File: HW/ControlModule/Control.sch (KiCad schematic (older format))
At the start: 81 parts, among them J1 Conn_01x03, J2 Conn_01x03, J3 Conn_01x03, J4 Conn_01x03, J5 Conn_01x03, J6 Conn_01x03, J7 Conn_01x03, J8 Conn_01x03, U1 AD8629, U2 STM32L476VETx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

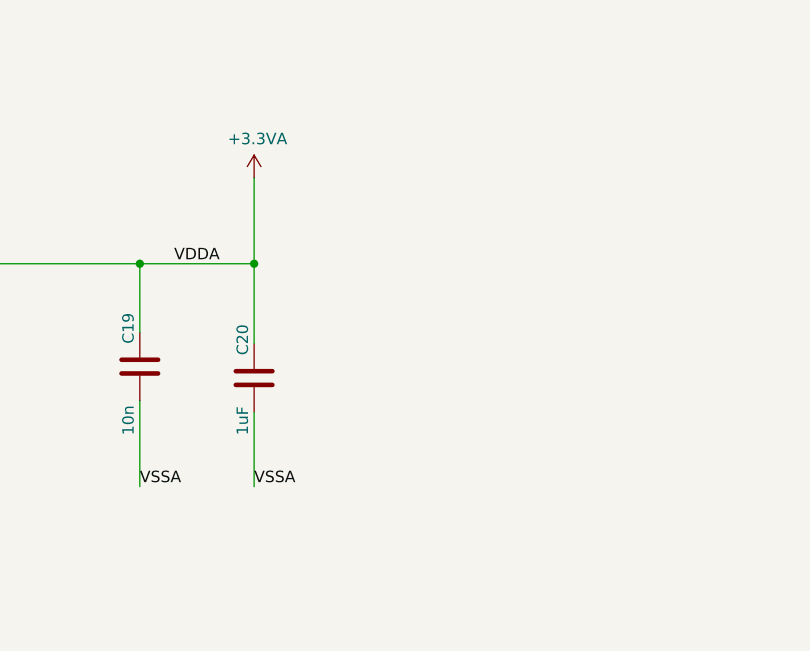
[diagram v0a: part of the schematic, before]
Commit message: Added Interafec IBOMS
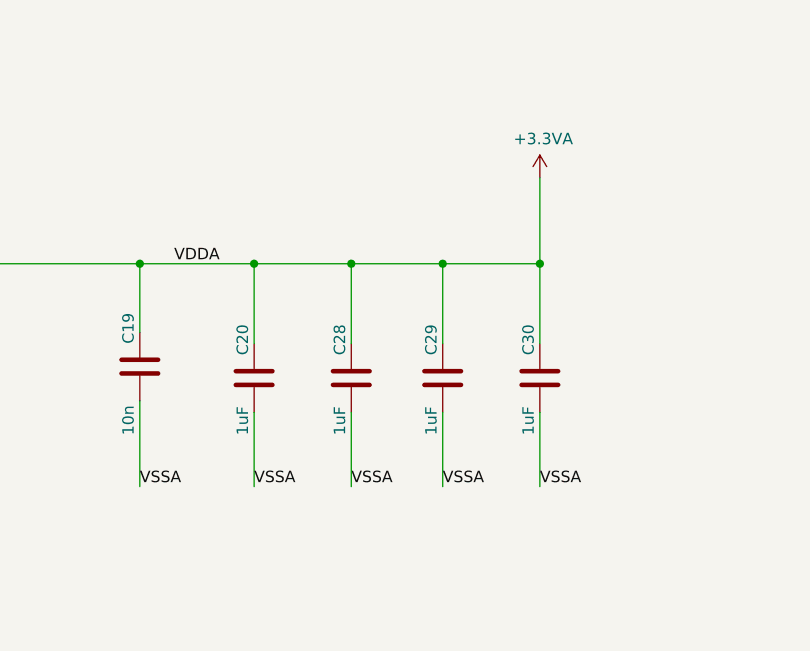
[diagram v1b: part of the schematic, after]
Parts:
- added C28, C29, C30: 1uF, Capacitor_SMD:C_0402_1005Metric, symbol Device:C
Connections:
- wire segments 308 -> 317
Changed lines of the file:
@@
 Connection ~ 10300 1650
-$Comp
-L power:+3.3VA #PWR030
-U 1 1 5E90E944
-P 14550 1450
-F 0 "#PWR030" H 14550 1300 50  0001 C CNN
-F 1 "+3.3VA" H 14565 1621 50  0000 C CNN
-F 2 "" H 14550 1450 50  0001 C CNN
-F 3 "" H 14550 1450 50  0001 C CNN
-	1    14550 1450
-	1    0    0    -1
-$EndComp
 $Comp
 L power:+3.3V #PWR012
@@
 	1    0    0    -1
 $EndComp
-Text Label 14200 1825 0    50   ~ 0
-VDDA
 Wire Wire Line
 	13100 1825 14050 1825
@@
 	14550 2475 14550 2800
 Wire Wire Line
-	14550 1450 14550 1825
-Wire Wire Line
 	10300 1550 10300 1650
 Wire Wire Line
@@
 Text Notes 7950 11850 0    197  ~ 0
 Voltage Regulator and Voltage Reference
+Wire Wire Line
+	14975 2475 14975 2800
+Text Label 14975 2800 0    50   ~ 0
+VSSA
+Wire Wire Line
+	14975 1825 14975 2175
+Wire Wire Line
+	15375 2475 15375 2800
+Text Label 15375 2800 0    50   ~ 0
+VSSA
+Wire Wire Line
+	15375 1825 15375 2175
+Wire Wire Line
+	15800 2475 15800 2800
+Text Label 15800 2800 0    50   ~ 0
+VSSA
+Wire Wire Line
+	15800 1825 15800 2175
+Wire Wire Line
+	14550 1825 14975 1825
+Connection ~ 14975 1825
+Wire Wire Line
+	14975 1825 15375 1825
+Connection ~ 15375 1825
+Wire Wire Line
+	15375 1825 15800 1825
+$Comp
+L Device:C C30
+U 1 1 5D5424B0
+P 15800 2325
+F 0 "C30" V 15750 2425 50  0000 L CNN
+F 1 "1uF" V 15750 2075 50  0000 L CNN
+F 2 "Capacitor_SMD:C_0402_1005Metric" H 15838 2175 50  0001 C CNN
+F 3 "~" H 15800 2325 50  0001 C CNN
+	1    15800 2325
+	1    0    0    -1
+$EndComp
+$Comp
+L Device:C C29
+U 1 1 5D527759
+P 15375 2325
+F 0 "C29" V 15325 2425 50  0000 L CNN
+F 1 "1uF" V 15325 2075 50  0000 L CNN
+F 2 "Capacitor_SMD:C_0402_1005Metric" H 15413 2175 50  0001 C CNN
+F 3 "~" H 15375 2325 50  0001 C CNN
+	1    15375 2325
+	1    0    0    -1
+$EndComp
+$Comp
+L Device:C C28
+U 1 1 5D50AF0D
+P 14975 2325
+F 0 "C28" V 14925 2425 50  0000 L CNN
+F 1 "1uF" V 14925 2075 50  0000 L CNN
+F 2 "Capacitor_SMD:C_0402_1005Metric" H 15013 2175 50  0001 C CNN
+F 3 "~" H 14975 2325 50  0001 C CNN
+	1    14975 2325
+	1    0    0    -1
+$EndComp
+Text Label 14200 1825 0    50   ~ 0
+VDDA
+Wire Wire Line
+	15800 1450 15800 1825
+$Comp
+L power:+3.3VA #PWR030
+U 1 1 5E90E944
+P 15800 1450
+F 0 "#PWR030" H 15800 1300 50  0001 C CNN
+F 1 "+3.3VA" H 15815 1621 50  0000 C CNN
+F 2 "" H 15800 1450 50  0001 C CNN
+F 3 "" H 15800 1450 50  0001 C CNN
+	1    15800 1450
+	1    0    0    -1
+$EndComp
+Connection ~ 15800 1825
 $EndSCHEMATC

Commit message: Created STM32L476 project
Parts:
- U_BTN1, U_BTN2, U_BTN3, U_BTN5: symbol Tactile_SPST-NO:Tactile_Switch_SPST-NO -> ControlModule-rescue:Tactile_Switch_SPST-NO-Tactile_SPST-NO
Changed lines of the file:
@@
 	19825 11300 19950 11300
 $Comp
-L Tactile_SPST-NO:Tactile_Switch_SPST-NO U_BTN3
+L ControlModule-rescue:Tactile_Switch_SPST-NO-Tactile_SPST-NO U_BTN3
 U 1 1 5CB3B653
 P 4600 13150
+AR Path="/5CB3B653" Ref="U_BTN3"  Part="1"
+AR Path="/5D061C98/5CB3B653" Ref="U_BTN3"  Part="1"
 F 0 "U_BTN3" H 4600 13550 50  0000 C CNN
 F 1 "Tactile_Switch_SPST-NO" H 4650 13450 50  0000 C CNN
@@
 NoConn ~ 5000 13250
 $Comp
-L Tactile_SPST-NO:Tactile_Switch_SPST-NO U_BTN5
+L ControlModule-rescue:Tactile_Switch_SPST-NO-Tactile_SPST-NO U_BTN5
 U 1 1 5CBE308F
 P 5850 13150
+AR Path="/5CBE308F" Ref="U_BTN5"  Part="1"
+AR Path="/5D061C98/5CBE308F" Ref="U_BTN5"  Part="1"
 F 0 "U_BTN5" H 5850 13550 50  0000 C CNN
 F 1 "Tactile_Switch_SPST-NO" H 5900 13450 50  0000 C CNN
@@
 NoConn ~ 6250 13250
 $Comp
-L Tactile_SPST-NO:Tactile_Switch_SPST-NO U_BTN2
+L ControlModule-rescue:Tactile_Switch_SPST-NO-Tactile_SPST-NO U_BTN2
 U 1 1 5CC20FAA
 P 2050 13150
+AR Path="/5CC20FAA" Ref="U_BTN2"  Part="1"
+AR Path="/5D061C98/5CC20FAA" Ref="U_BTN2"  Part="1"
 F 0 "U_BTN2" H 2050 13550 50  0000 C CNN
 F 1 "Tactile_Switch_SPST-NO" H 2100 13450 50  0000 C CNN
@@
 NoConn ~ 2450 13250
 $Comp
-L Tactile_SPST-NO:Tactile_Switch_SPST-NO U_BTN1
+L ControlModule-rescue:Tactile_Switch_SPST-NO-Tactile_SPST-NO U_BTN1
 U 1 1 5CC42781
 P 3350 13150
+AR Path="/5CC42781" Ref="U_BTN1"  Part="1"
+AR Path="/5D061C98/5CC42781" Ref="U_BTN1"  Part="1"
 F 0 "U_BTN1" H 3350 13550 50  0000 C CNN
 F 1 "Tactile_Switch_SPST-NO" H 3400 13450 50  0000 C CNN

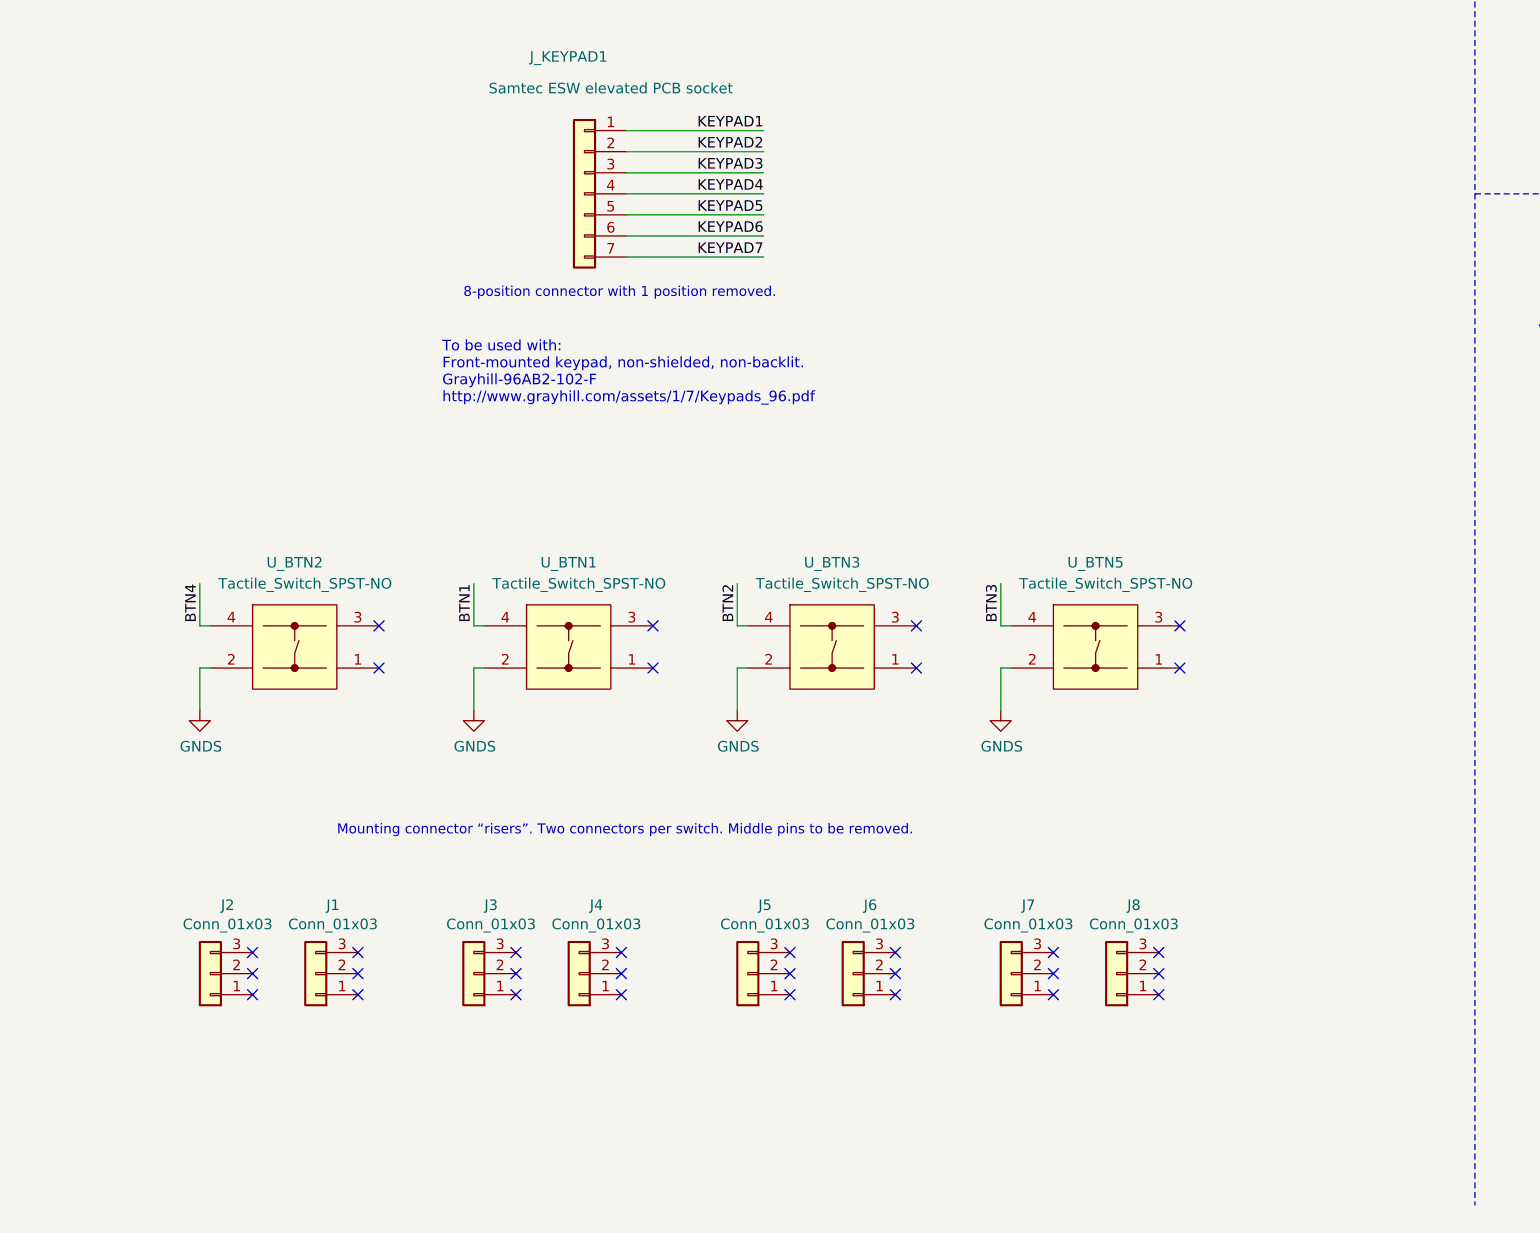
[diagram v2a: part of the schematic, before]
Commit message: debugged HW issue with EXTI buttons
- Buttons required external pull-up resistors
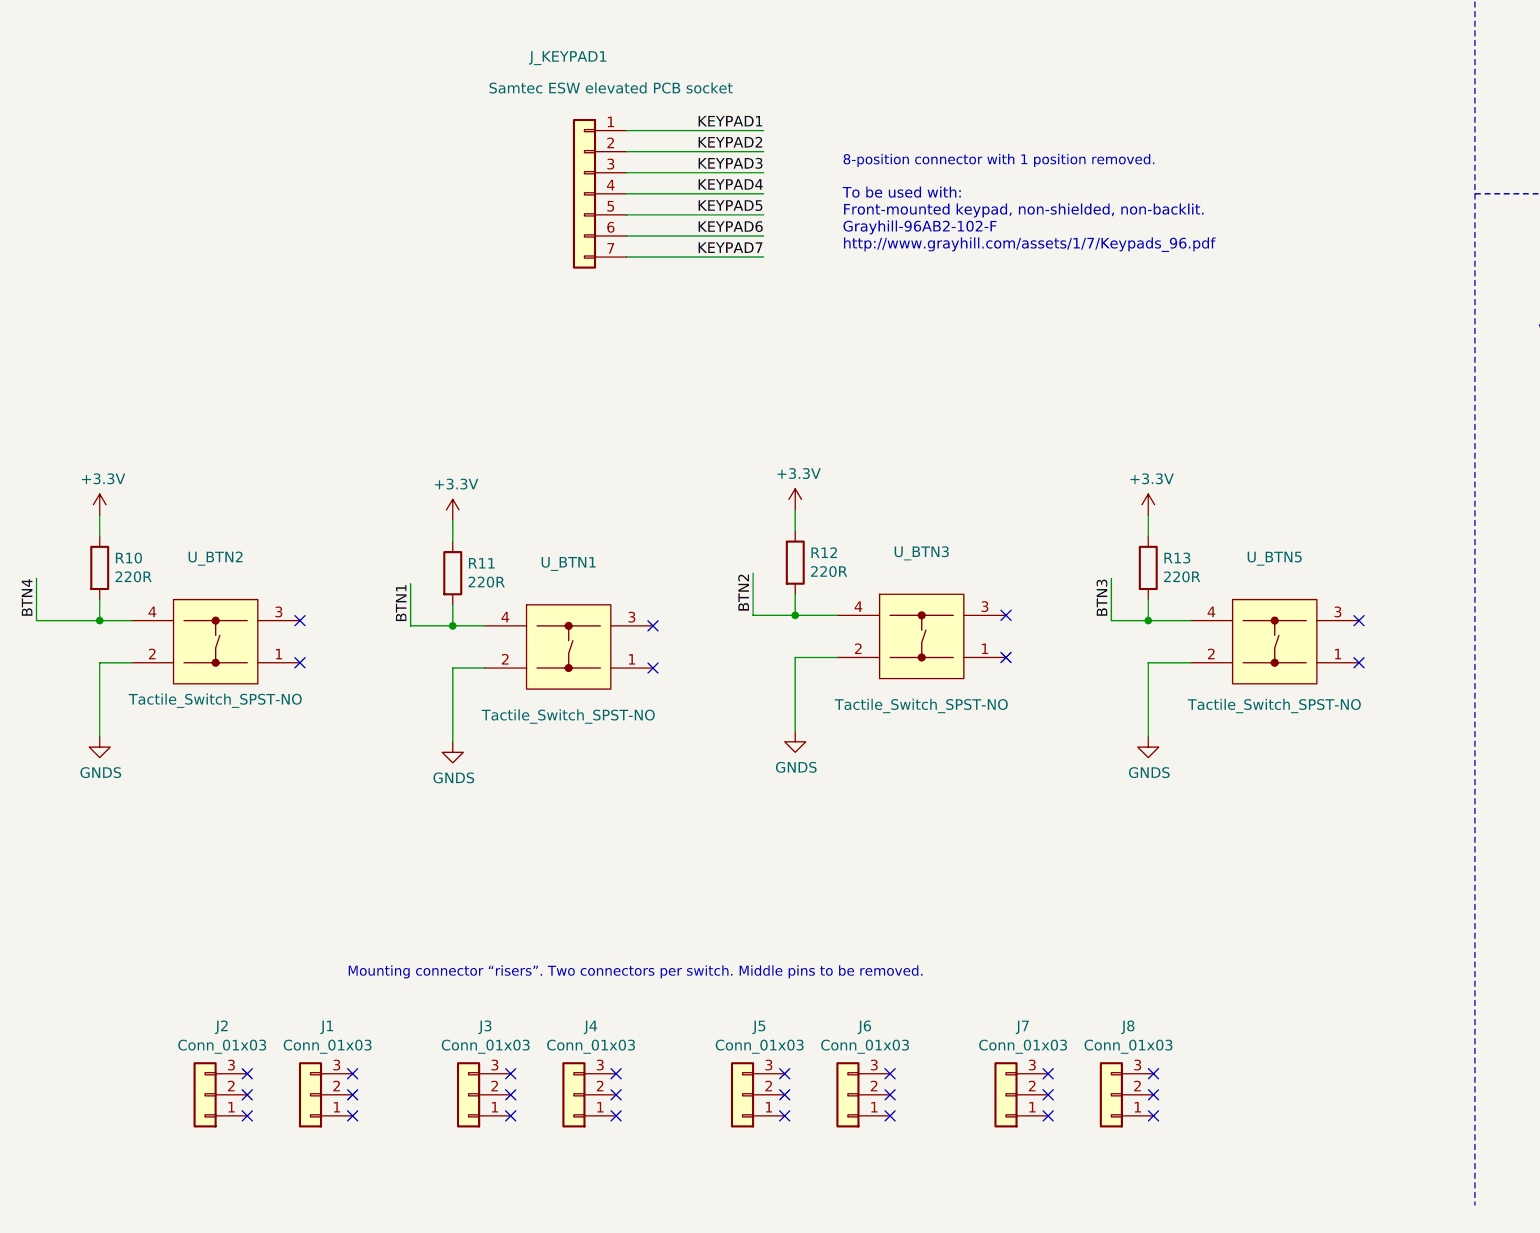
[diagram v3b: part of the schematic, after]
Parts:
- added R10, R11, R12, R13: 220R, Resistor_SMD:R_0805_2012Metric_Pad1.15x1.40mm_HandSolder, symbol Device:R
- C17, C18, C21, C22: footprint Capacitor_SMD:C_0402_1005Metric -> Capacitor_SMD:C_0805_2012Metric_Pad1.15x1.40mm_HandSolder
- L1, L2: footprint Resistor_SMD:R_0402_1005Metric -> Resistor_SMD:R_0805_2012Metric_Pad1.15x1.40mm_HandSolder
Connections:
- net +3V3: now also R10.1, R11.1, R12.1, R13.1
- net BTN1: now also R11.2
- net BTN2: now also R12.2
- net BTN3: now also R13.2
- net BTN4: now also R10.2
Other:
- moved on the sheet: J1, J2, J3, J4, J5, J6, J7, J8, U_BTN2, U_BTN3, U_BTN5

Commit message: updated SW
- Tested HW with ADC enabled. Basic SWDIO debug data received (with unexpected 200mV offset)
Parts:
- removed JP5, JP6: BYPASS, Jumper:SolderJumper-2_P1.3mm_Open_Pad1.0x1.5mm, symbol Device:Jumper_NO_Small
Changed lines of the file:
@@
 Wire Wire Line
 	4100 3350 4100 3150
-Wire Wire Line
-	4100 3150 4400 3150
 $Comp
 L Device:R R2
@@
 Connection ~ 4100 5950
 Wire Wire Line
-	4100 5950 4400 5950
-Wire Wire Line
 	4100 6450 4100 7700
 Connection ~ 4100 7700
-$Comp
-L Device:Jumper_NO_Small JP5
-U 1 1 5D9A48A0
-P 5300 4450
-F 0 "JP5" H 5300 4550 50  0000 C CNN
-F 1 "BYPASS" H 5300 4350 50  0000 C CNN
-F 2 "Jumper:SolderJumper-2_P1.3mm_Open_Pad1.0x1.5mm" H 5300 4450 50  0001 C CNN
-F 3 "~" H 5300 4450 50  0001 C CNN
-	1    5300 4450
-	1    0    0    -1
-$EndComp
-Wire Wire Line
-	5200 4450 4400 4450
-Wire Wire Line
-	4400 4450 4400 3150
-Connection ~ 4400 3150
-Wire Wire Line
-	4400 3150 5000 3150
-Wire Wire Line
-	5400 4450 5900 4450
-Wire Wire Line
-	5900 4450 5900 3250
-$Comp
-L Device:Jumper_NO_Small JP6
-U 1 1 5DA126C3
-P 5300 7300
-F 0 "JP6" H 5300 7375 50  0000 C CNN
-F 1 "BYPASS" H 5300 7225 50  0000 C CNN
-F 2 "Jumper:SolderJumper-2_P1.3mm_Open_Pad1.0x1.5mm" H 5300 7300 50  0001 C CNN
-F 3 "~" H 5300 7300 50  0001 C CNN
-	1    5300 7300
-	1    0    0    -1
-$EndComp
-Wire Wire Line
-	5200 7300 4400 7300
-Wire Wire Line
-	4400 7300 4400 5950
-Connection ~ 4400 5950
-Wire Wire Line
-	4400 5950 4950 5950
-Wire Wire Line
-	5400 7300 5900 7300
-Wire Wire Line
-	5900 7300 5900 6050
 $Bitmap
 Pos 2300 3700
@@
 Wire Wire Line
 	2800 13050 2600 13050
+Wire Wire Line
+	4100 3150 5000 3150
+Wire Wire Line
+	4100 5950 4950 5950
 $EndSCHEMATC

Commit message: updated
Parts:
- added JP5, JP6: BYPASS, Jumper:SolderJumper-2_P1.3mm_Open_Pad1.0x1.5mm, symbol Device:Jumper_NO_Small
- C26, C27: value 1u -> 10pF
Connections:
- net ADCS1: now also JP5.2
- net ADCS2: now also JP6.2
- net at C1.1, R3.1, U1.3 (+): now also JP5.1
- net at C2.2, R4.1, U1.5 (+): now also JP6.1
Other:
- note added: "TO BYPASS:\n1) Remove U1\n2) Solder JP5, JP6, R1 and R2\n3) Populate R3, R4 with 10K\nand C1, C2 with 1uF for FC=15Hz"

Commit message: Tested Contrl Module ADC input filter. Updated schematic for removing >1MHz noise.
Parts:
- C1, C2: value 1u -> 100nF
- C26: value 10pF -> 0F
- C27: value 10pF -> oF
- C3, C4: value 1u -> 0F
- R1, R2, R8, R9: value 10K -> 0R
- R3, R4: value 10K -> 100R
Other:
- note added: "TO BYPASS:\n1) Remove U1\n2) Solder JP5, JP6, R1 and R2\n3) Populate R3, R4 with 100R\nand C1, C2 with 100nF for FC=15KHz"
- note removed: "TO BYPASS:\n1) Remove U1\n2) Solder JP5, JP6, R1 and R2\n3) Populate R3, R4 with 10K\nand C1, C2 with 1uF for FC=15Hz"
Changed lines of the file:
@@
 P 3750 3150
 F 0 "R3" V 3543 3150 50  0000 C CNN
-F 1 "10K" V 3634 3150 50  0000 C CNN
+F 1 "100R" V 3634 3150 50  0000 C CNN
 F 2 "Resistor_SMD:R_0402_1005Metric" V 3680 3150 50  0001 C CNN
 F 3 "~" H 3750 3150 50  0001 C CNN
@@
 P 4750 2650
 F 0 "C3" V 5000 2600 50  0000 L CNN
-F 1 "1u" V 4900 2600 50  0000 L CNN
+F 1 "0F" V 4900 2600 50  0000 L CNN
 F 2 "Capacitor_SMD:C_0402_1005Metric" H 4788 2500 50  0001 C CNN
 F 3 "~" H 4750 2650 50  0001 C CNN
@@
 P 3200 5950
 F 0 "R1" V 2993 5950 50  0000 C CNN
-F 1 "10K" V 3084 5950 50  0000 C CNN
+F 1 "0R" V 3084 5950 50  0000 C CNN
 F 2 "Resistor_SMD:R_0402_1005Metric" V 3130 5950 50  0001 C CNN
 F 3 "~" H 3200 5950 50  0001 C CNN
@@
 P 4750 5350
 F 0 "C4" V 4500 5300 50  0000 L CNN
-F 1 "1u" V 4600 5350 50  0000 L CNN
+F 1 "0F" V 4600 5350 50  0000 L CNN
 F 2 "Capacitor_SMD:C_0402_1005Metric" H 4788 5200 50  0001 C CNN
 F 3 "~" H 4750 5350 50  0001 C CNN
@@
 P 4100 3500
 F 0 "C1" H 3900 3550 50  0000 L CNN
-F 1 "1u" H 3900 3450 50  0000 L CNN
+F 1 "100nF" H 3900 3450 50  0000 L CNN
 F 2 "Capacitor_SMD:C_0402_1005Metric" H 4138 3350 50  0001 C CNN
 F 3 "~" H 4100 3500 50  0001 C CNN
@@
 P 3250 3150
 F 0 "R2" V 3043 3150 50  0000 C CNN
-F 1 "10K" V 3134 3150 50  0000 C CNN
+F 1 "0R" V 3134 3150 50  0000 C CNN
 F 2 "Resistor_SMD:R_0402_1005Metric" V 3180 3150 50  0001 C CNN
 F 3 "~" H 3250 3150 50  0001 C CNN
@@
 P 3750 5950
 F 0 "R4" V 3543 5950 50  0000 C CNN
-F 1 "10K" V 3634 5950 50  0000 C CNN
+F 1 "100R" V 3634 5950 50  0000 C CNN
 F 2 "Resistor_SMD:R_0402_1005Metric" V 3680 5950 50  0001 C CNN
 F 3 "~" H 3750 5950 50  0001 C CNN
@@
 P 4100 6300
 F 0 "C2" H 4215 6346 50  0000 L CNN
-F 1 "1u" H 4215 6255 50  0000 L CNN
+F 1 "100nF" H 4215 6255 50  0000 L CNN
 F 2 "Capacitor_SMD:C_0402_1005Metric" H 4138 6150 50  0001 C CNN
 F 3 "~" H 4100 6300 50  0001 C CNN
@@
 P 5250 3800
 F 0 "R8" V 5125 3600 50  0000 C CNN
-F 1 "10K" V 5125 3950 50  0000 C CNN
+F 1 "0R" V 5125 3950 50  0000 C CNN
 F 2 "Resistor_SMD:R_0402_1005Metric" V 5180 3800 50  0001 C CNN
 F 3 "~" H 5250 3800 50  0001 C CNN
@@
 P 5250 4000
 F 0 "C26" V 5050 4100 50  0000 L CNN
-F 1 "10pF" V 5050 3800 50  0000 L CNN
+F 1 "0F" V 5050 3800 50  0000 L CNN
 F 2 "Capacitor_SMD:C_0402_1005Metric" H 5288 3850 50  0001 C CNN
 F 3 "~" H 5250 4000 50  0001 C CNN
@@
 P 5250 6600
 F 0 "R9" V 5125 6400 50  0000 C CNN
-F 1 "10K" V 5125 6750 50  0000 C CNN
+F 1 "0R" V 5125 6750 50  0000 C CNN
 F 2 "Resistor_SMD:R_0402_1005Metric" V 5180 6600 50  0001 C CNN
 F 3 "~" H 5250 6600 50  0001 C CNN
@@
 P 5250 6800
 F 0 "C27" V 5050 6900 50  0000 L CNN
-F 1 "10pF" V 5050 6550 50  0000 L CNN
+F 1 "oF" V 5050 6550 50  0000 L CNN
 F 2 "Capacitor_SMD:C_0402_1005Metric" H 5288 6650 50  0001 C CNN
 F 3 "~" H 5250 6800 50  0001 C CNN
@@
 	5900 7400 5900 6050
 Text Notes 1550 4400 0    50   ~ 0
-TO BYPASS:\n1) Remove U1\n2) Solder JP5, JP6, R1 and R2\n3) Populate R3, R4 with 10K\nand C1, C2 with 1uF for FC=15Hz
+TO BYPASS:\n1) Remove U1\n2) Solder JP5, JP6, R1 and R2\n3) Populate R3, R4 with 100R\nand C1, C2 with 100nF for FC=15KHz
 $EndSCHEMATC
